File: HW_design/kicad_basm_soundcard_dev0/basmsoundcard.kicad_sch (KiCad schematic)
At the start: 1 part

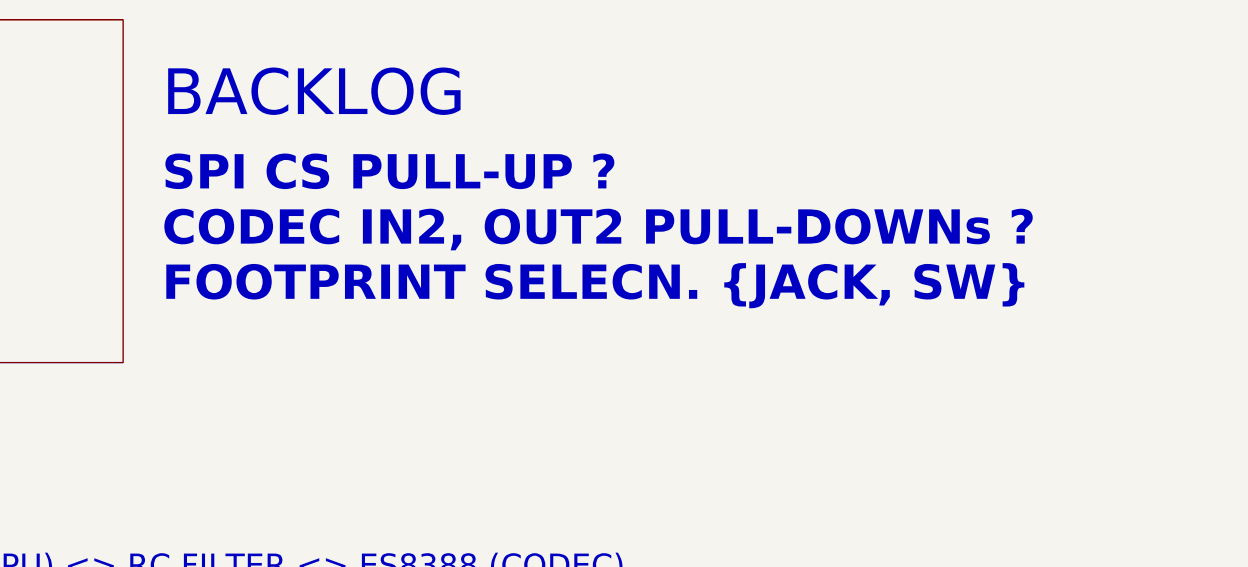
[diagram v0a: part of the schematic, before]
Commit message: Changed Footprints for LED RGB, SD, AudioJack, USB
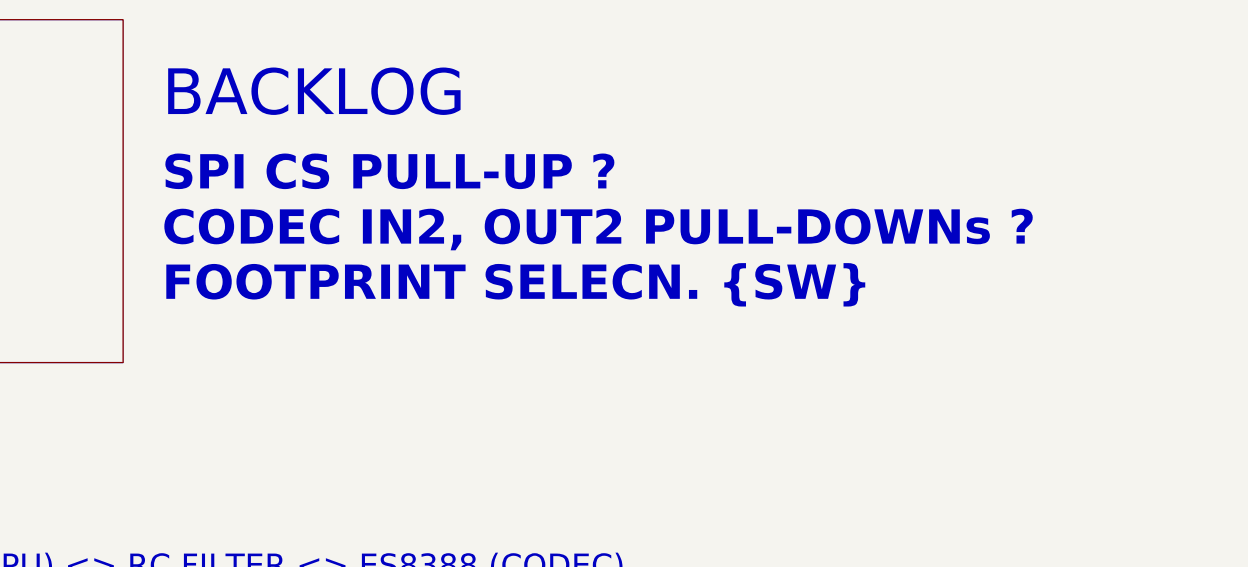
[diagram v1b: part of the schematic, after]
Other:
- note added: "SPI CS PULL-UP ? CODEC IN2, OUT2 PULL-DOWNs ? FOOTPRINT SELECN. {SW}"
- note removed: "SPI CS PULL-UP ? CODEC IN2, OUT2 PULL-DOWNs ? FOOTPRINT SELECN. {JACK, SW}"
- company: (none) -> BUCHAREST APPLIED STEAM MUSEUM
- title: (none) -> BASM SOUNDCARD
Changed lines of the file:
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@@
 	(generator_version "8.0")
 	(paper "A4")
+	(title_block
+		(title "BASM SOUNDCARD")
+		(rev "1")
+		(company "BUCHAREST APPLIED STEAM MUSEUM")
+		(comment 1 "Changed 10u Cap. Footprints to 0603")
+	)
 	(rectangle
 		(start 203.2 30.48)
@@
 		)
 	)
-	(text "SPI CS PULL-UP ?\nCODEC IN2, OUT2 PULL-DOWNs ?\nFOOTPRINT SELECN. {JACK, SW}"
+	(text "SPI CS PULL-UP ?\nCODEC IN2, OUT2 PULL-DOWNs ?\nFOOTPRINT SELECN. {SW}"
 		(exclude_from_sim no)
 		(at 183.388 116.078 0)
